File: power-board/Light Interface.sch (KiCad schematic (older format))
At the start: 20 parts, among them J3 CONN_01X04, J4 CONN_01X04, J5 CONN_01X04, J6 CONN_01X04, J7 CONN_01X04

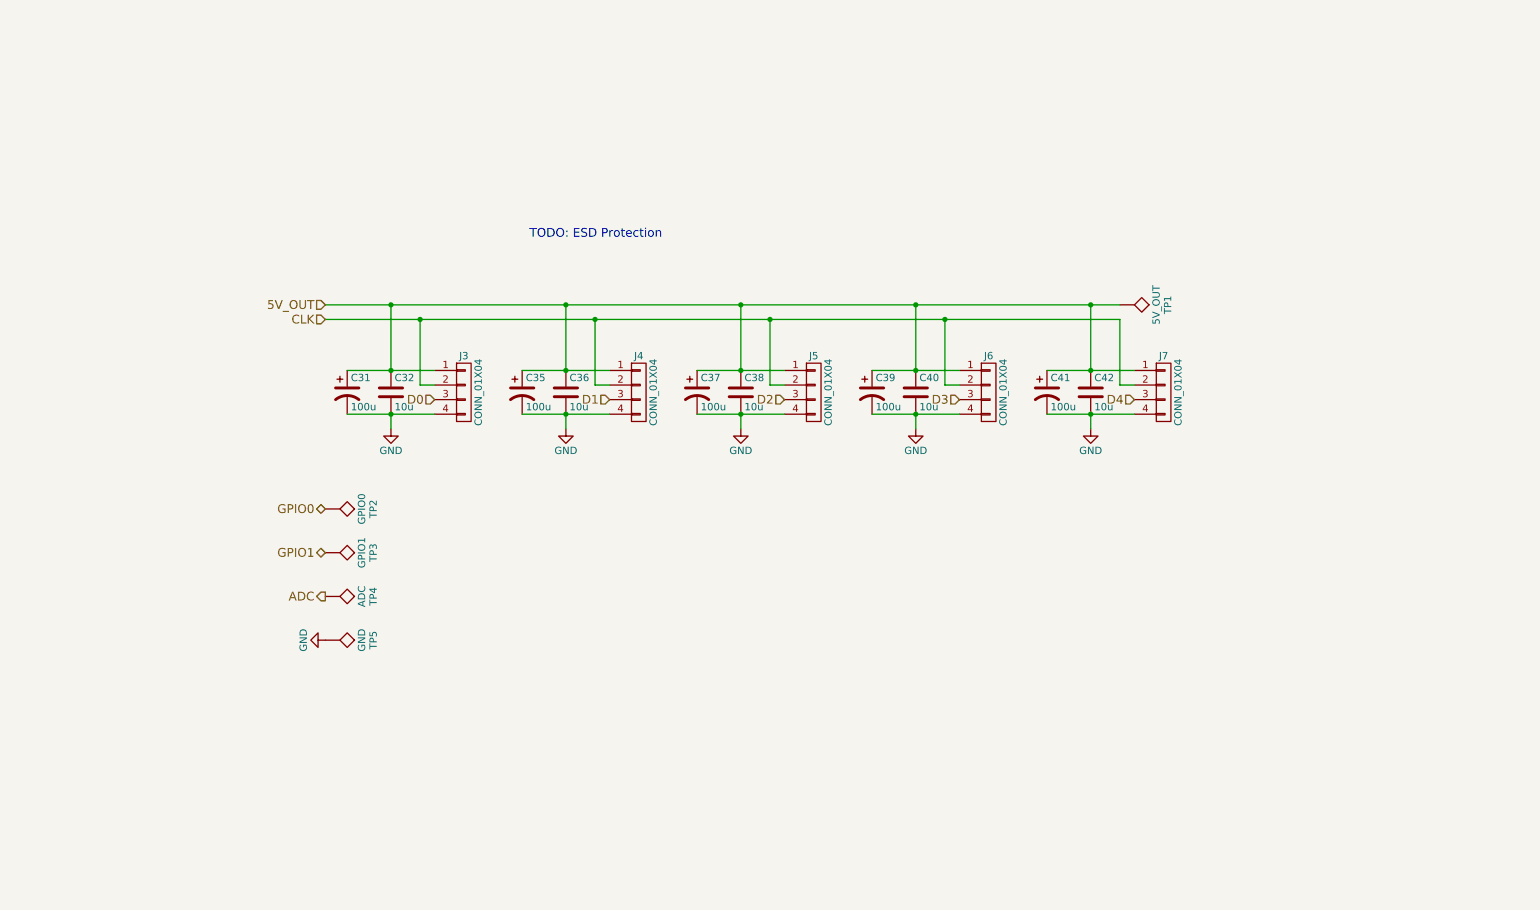
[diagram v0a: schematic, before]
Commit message: changed MCU to run at 3.3v
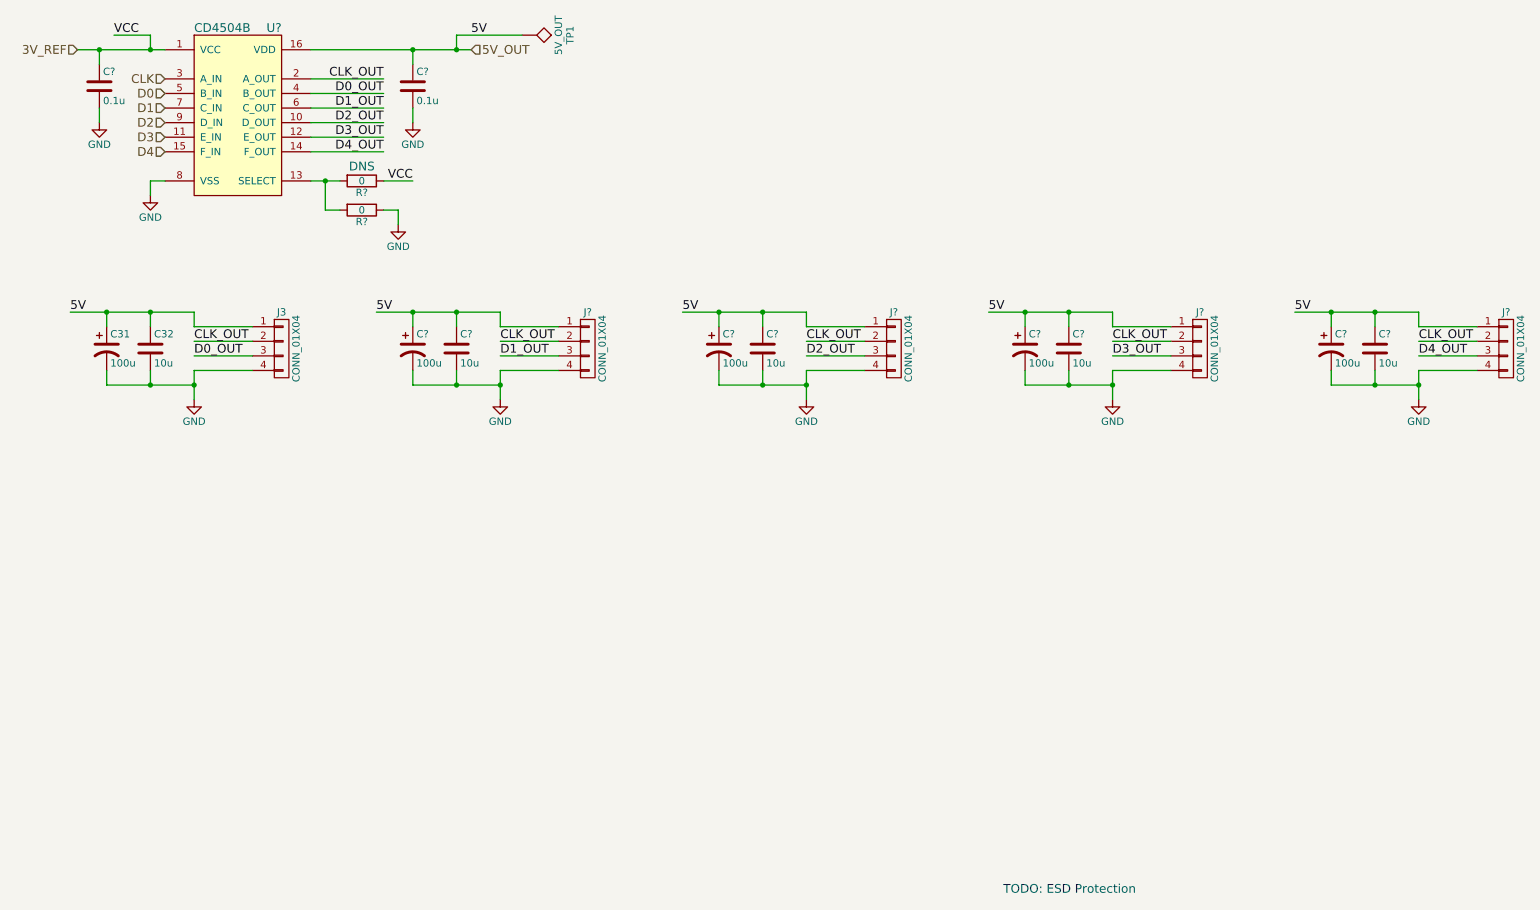
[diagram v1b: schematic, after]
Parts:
- removed C35, C37, C39, C41: 100u, symbol CP1
- removed C36, C38, C40, C42: 10u, symbol C
- removed J4, J5, J6, J7: CONN_01X04, symbol CONN_01X04
- removed TP2: GPIO0, symbol TEST
- removed TP3: GPIO1, symbol TEST
- removed TP4: ADC, symbol TEST
- removed TP5: GND, symbol TEST
- added C? (x2): 0.1u, symbol C
- added C? (x4): 10u, symbol C
- added C? (x4): 100u, symbol CP1
- added J? (x4): CONN_01X04, symbol CONN_01X04
- added R? (x2): 0, symbol R
- added U?: CD4504B, symbol CD4504B
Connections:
- net 5V_OUT: now also C?.1, C?.1, C?.1, C?.1, C?.1, C?.1, C?.1, C?.1, C?.1, J?.1 (P1), J?.1 (P1), J?.1 (P1), J?.1 (P1), U?.16 (VDD)
- net CLK: now also U?.3 (A_IN); no longer J3.2 (P2)
- net D0: now also U?.5 (B_IN); no longer J3.3 (P3)
- net D1: now also U?.7 (C_IN)
- net D2: now also U?.9 (D_IN)
- net D3: now also U?.11 (E_IN)
- net D4: now also U?.15 (F_IN)
- net GND: now also C?.2, C?.2, C?.2, C?.2, C?.2, C?.2, C?.2, C?.2, C?.2, C?.2, J?.4 (P4), J?.4 (P4), J?.4 (P4), J?.4 (P4), R?.1, U?.8 (VSS)
- new net: R?.2, R?.2, U?.13 (SELECT)
- new net 3V_REF: C?.1, R?.1, U?.1 (VCC)
- new net CLK_OUT: J3.2 (P2), J?.2 (P2), J?.2 (P2), J?.2 (P2), J?.2 (P2), U?.2 (A_OUT)
- new net D0_OUT: J3.3 (P3), U?.4 (B_OUT)
- new net D1_OUT: J?.3 (P3), U?.6 (C_OUT)
- new net D2_OUT: J?.3 (P3), U?.10 (D_OUT)
- new net D3_OUT: J?.3 (P3), U?.12 (E_OUT)
- new net D4_OUT: J?.3 (P3), U?.14 (F_OUT)
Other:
- moved on the sheet: C31, C32, J3, TP1

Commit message: switched to XMEGA A4U
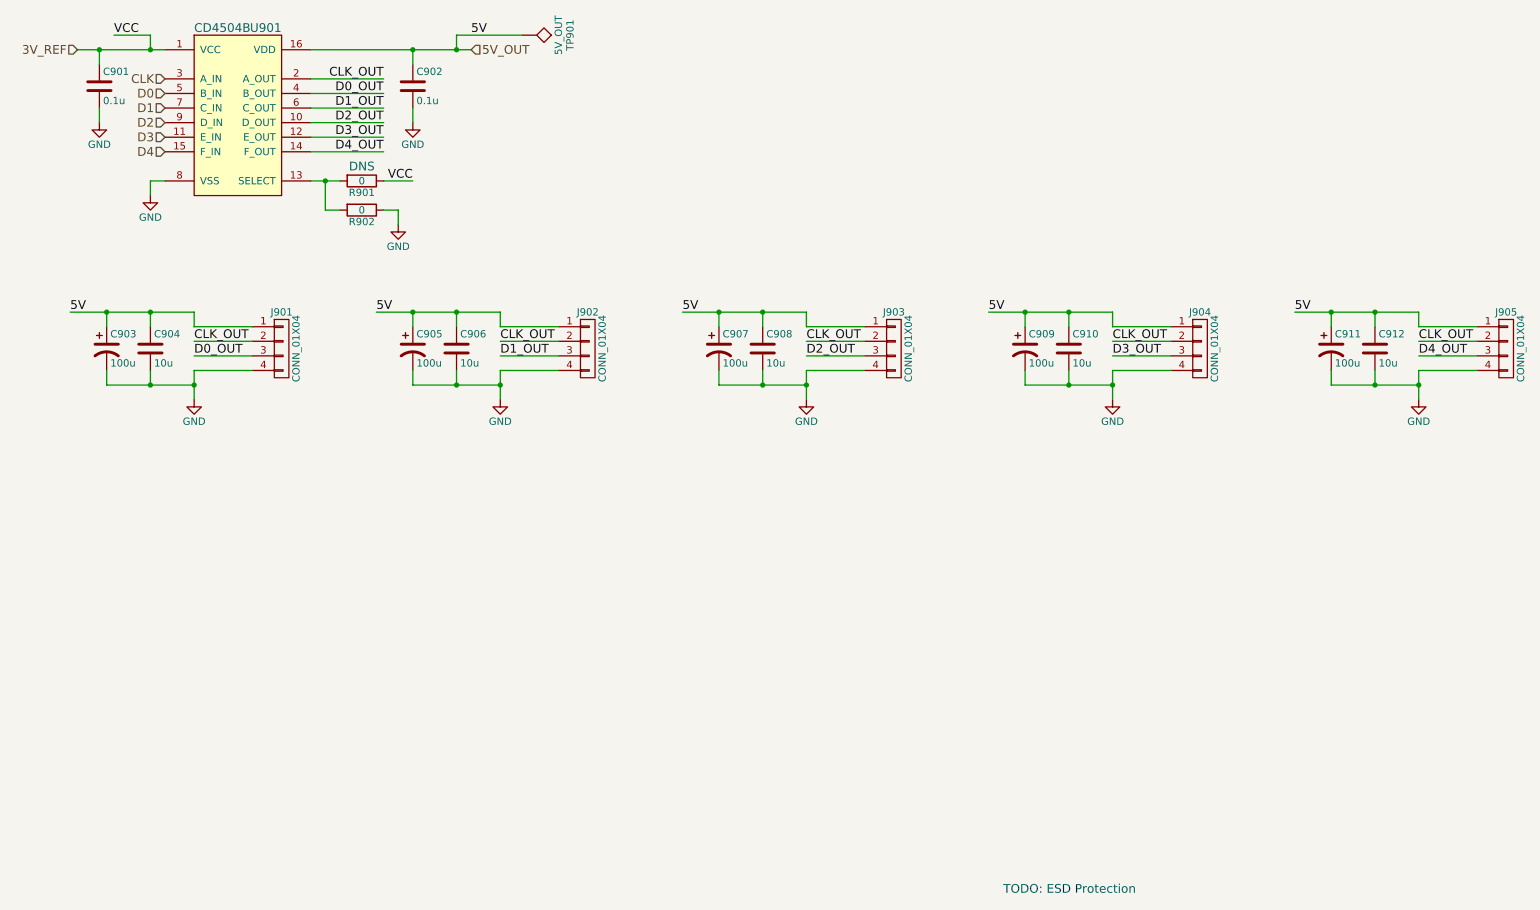
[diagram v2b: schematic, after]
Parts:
- gave numbers to parts that had none: 17
- renumbered C31 to C903, C32 to C904, J3 to J901, TP1 to TP901
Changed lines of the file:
@@
 $Descr A4 11693 8268
 encoding utf-8
-Sheet 9 10
+Sheet 9 11
 Title ""
 Date ""
@@
 CLK
 $Comp
-L CONN_01X04 J3
+L CONN_01X04 J901
 U 1 1 593A4988
 P 2300 2950
-F 0 "J3" H 2300 3200 50  0000 C CNN
+F 0 "J901" H 2300 3200 50  0000 C CNN
 F 1 "CONN_01X04" V 2400 2950 50  0000 C CNN
 F 2 "" H 2300 2950 50  0001 C CNN
@@
 $EndComp
 $Comp
-L C C32
+L C C904
 U 1 1 593A49E6
 P 1400 2950
-F 0 "C32" H 1425 3050 50  0000 L CNN
+F 0 "C904" H 1425 3050 50  0000 L CNN
 F 1 "10u" H 1425 2850 50  0000 L CNN
 F 2 "" H 1438 2800 50  0001 C CNN
@@
 $EndComp
 $Comp
-L CP1 C31
+L CP1 C903
 U 1 1 593A4A03
 P 1100 2950
-F 0 "C31" H 1125 3050 50  0000 L CNN
+F 0 "C903" H 1125 3050 50  0000 L CNN
 F 1 "100u" H 1125 2850 50  0000 L CNN
 F 2 "" H 1100 2950 50  0001 C CNN
@@
 $EndComp
 $Comp
-L GND #PWR37
+L GND #PWR045
 U 1 1 593A4A49
 P 1700 3300
-F 0 "#PWR37" H 1700 3050 50  0001 C CNN
+F 0 "#PWR045" H 1700 3050 50  0001 C CNN
 F 1 "GND" H 1700 3150 50  0000 C CNN
 F 2 "" H 1700 3300 50  0001 C CNN
@@
 	2100 2900 1700 2900
 $Comp
-L TEST TP1
+L TEST TP901
 U 1 1 593A5C05
 P 3950 800
-F 0 "TP1" H 3950 1100 50  0000 C BNN
+F 0 "TP901" H 3950 1100 50  0000 C BNN
 F 1 "5V_OUT" H 3950 1050 50  0000 C CNN
 F 2 "" H 3950 800 50  0001 C CNN
@@
 3V_REF
 $Comp
-L CD4504B U?
+L CD4504B U901
 U 1 1 593C5912
 P 1700 800
-F 0 "U?" H 2300 850 60  0000 R CNN
+F 0 "U901" H 2300 850 60  0000 R CNN
 F 1 "CD4504B" H 1700 850 60  0000 L CNN
 F 2 "" H 1750 950 60  0001 C CNN
@@
 	2100 2800 1700 2800
 Wire Wire Line
-	1700 2700 1700 2800
-Wire Wire Line
-	850  2700 1700 2700
+	1700 2800 1700 2700
+Wire Wire Line
+	1700 2700 850  2700
 Wire Wire Line
 	2100 3100 1700 3100
@@
 D4
 $Comp
-L GND #PWR?
+L GND #PWR046
 U 1 1 593C6AA7
 P 1400 1900
-F 0 "#PWR?" H 1400 1650 50  0001 C CNN
+F 0 "#PWR046" H 1400 1650 50  0001 C CNN
 F 1 "GND" H 1400 1750 50  0000 C CNN
 F 2 "" H 1400 1900 50  0001 C CNN
@@
 	1400 1800 1500 1800
 $Comp
-L C C?
+L C C901
 U 1 1 593C6AF5
 P 1050 1150
-F 0 "C?" H 1075 1250 50  0000 L CNN
+F 0 "C901" H 1075 1250 50  0000 L CNN
 F 1 "0.1u" H 1075 1050 50  0000 L CNN
 F 2 "" H 1088 1000 50  0001 C CNN
@@
 $EndComp
 $Comp
-L GND #PWR?
+L GND #PWR047
 U 1 1 593C6B4C
 P 1050 1400
-F 0 "#PWR?" H 1050 1150 50  0001 C CNN
+F 0 "#PWR047" H 1050 1150 50  0001 C CNN
 F 1 "GND" H 1050 1250 50  0000 C CNN
 F 2 "" H 1050 1400 50  0001 C CNN
@@
 Connection ~ 1050 900
 $Comp
-L C C?
+L C C902
 U 1 1 593C6C08
 P 3200 1150
-F 0 "C?" H 3225 1250 50  0000 L CNN
+F 0 "C902" H 3225 1250 50  0000 L CNN
 F 1 "0.1u" H 3225 1050 50  0000 L CNN
 F 2 "" H 3238 1000 50  0001 C CNN
@@
 $EndComp
 $Comp
-L GND #PWR?
+L GND #PWR048
 U 1 1 593C6C0E
 P 3200 1400
-F 0 "#PWR?" H 3200 1150 50  0001 C CNN
+F 0 "#PWR048" H 3200 1150 50  0001 C CNN
 F 1 "GND" H 3200 1250 50  0000 C CNN
 F 2 "" H 3200 1400 50  0001 C CNN
@@
 	3000 1600 2500 1600
 $Comp
-L CONN_01X04 J?
+L CONN_01X04 J902
 U 1 1 593C76E0
 P 4400 2950
-F 0 "J?" H 4400 3200 50  0000 C CNN
+F 0 "J902" H 4400 3200 50  0000 C CNN
 F 1 "CONN_01X04" V 4500 2950 50  0000 C CNN
 F 2 "" H 4400 2950 50  0001 C CNN
@@
 $EndComp
 $Comp
-L C C?
+L C C906
 U 1 1 593C76E8
 P 3500 2950
-F 0 "C?" H 3525 3050 50  0000 L CNN
+F 0 "C906" H 3525 3050 50  0000 L CNN
 F 1 "10u" H 3525 2850 50  0000 L CNN
 F 2 "" H 3538 2800 50  0001 C CNN
@@
 $EndComp
 $Comp
-L CP1 C?
+L CP1 C905
 U 1 1 593C76F0
 P 3200 2950
-F 0 "C?" H 3225 3050 50  0000 L CNN
+F 0 "C905" H 3225 3050 50  0000 L CNN
 F 1 "100u" H 3225 2850 50  0000 L CNN
 F 2 "" H 3200 2950 50  0001 C CNN
@@
 $EndComp
 $Comp
-L GND #PWR?
+L GND #PWR049
 U 1 1 593C76F6
 P 3800 3300
-F 0 "#PWR?" H 3800 3050 50  0001 C CNN
+F 0 "#PWR049" H 3800 3050 50  0001 C CNN
 F 1 "GND" H 3800 3150 50  0000 C CNN
 F 2 "" H 3800 3300 50  0001 C CNN
@@
 	4200 2800 3800 2800
 Wire Wire Line
-	3800 2700 3800 2800
-Wire Wire Line
-	2950 2700 3800 2700
+	3800 2800 3800 2700
+Wire Wire Line
+	3800 2700 2950 2700
 Wire Wire Line
 	4200 3100 3800 3100
@@
 D1_OUT
 $Comp
-L CONN_01X04 J?
+L CONN_01X04 J903
 U 1 1 593C797D
 P 6500 2950
-F 0 "J?" H 6500 3200 50  0000 C CNN
+F 0 "J903" H 6500 3200 50  0000 C CNN
 F 1 "CONN_01X04" V 6600 2950 50  0000 C CNN
 F 2 "" H 6500 2950 50  0001 C CNN
@@
 $EndComp
 $Comp
-L C C?
+L C C908
 U 1 1 593C7985
 P 5600 2950
-F 0 "C?" H 5625 3050 50  0000 L CNN
+F 0 "C908" H 5625 3050 50  0000 L CNN
 F 1 "10u" H 5625 2850 50  0000 L CNN
 F 2 "" H 5638 2800 50  0001 C CNN
@@
 $EndComp
 $Comp
-L CP1 C?
+L CP1 C907
 U 1 1 593C798D
 P 5300 2950
-F 0 "C?" H 5325 3050 50  0000 L CNN
+F 0 "C907" H 5325 3050 50  0000 L CNN
 F 1 "100u" H 5325 2850 50  0000 L CNN
 F 2 "" H 5300 2950 50  0001 C CNN
@@
 $EndComp
 $Comp
-L GND #PWR?
+L GND #PWR050
 U 1 1 593C7993
 P 5900 3300
-F 0 "#PWR?" H 5900 3050 50  0001 C CNN
+F 0 "#PWR050" H 5900 3050 50  0001 C CNN
 F 1 "GND" H 5900 3150 50  0000 C CNN
 F 2 "" H 5900 3300 50  0001 C CNN
@@
 	6300 2800 5900 2800
 Wire Wire Line
-	5900 2700 5900 2800
-Wire Wire Line
-	5050 2700 5900 2700
+	5900 2800 5900 2700
+Wire Wire Line
+	5900 2700 5050 2700
 Wire Wire Line
 	6300 3100 5900 3100
@@
 D2_OUT
 $Comp
-L CONN_01X04 J?
+L CONN_01X04 J904
 U 1 1 593C79B0
 P 8600 2950
-F 0 "J?" H 8600 3200 50  0000 C CNN
+F 0 "J904" H 8600 3200 50  0000 C CNN
 F 1 "CONN_01X04" V 8700 2950 50  0000 C CNN
 F 2 "" H 8600 2950 50  0001 C CNN
@@
 $EndComp
 $Comp
-L C C?
+L C C910
 U 1 1 593C79B8
 P 7700 2950
-F 0 "C?" H 7725 3050 50  0000 L CNN
+F 0 "C910" H 7725 3050 50  0000 L CNN
 F 1 "10u" H 7725 2850 50  0000 L CNN
 F 2 "" H 7738 2800 50  0001 C CNN
@@
 $EndComp
 $Comp
-L CP1 C?
+L CP1 C909
 U 1 1 593C79C0
 P 7400 2950
-F 0 "C?" H 7425 3050 50  0000 L CNN
+F 0 "C909" H 7425 3050 50  0000 L CNN
 F 1 "100u" H 7425 2850 50  0000 L CNN
 F 2 "" H 7400 2950 50  0001 C CNN
@@
 $EndComp
 $Comp
-L GND #PWR?
+L GND #PWR051
 U 1 1 593C79C6
 P 8000 3300
-F 0 "#PWR?" H 8000 3050 50  0001 C CNN
+F 0 "#PWR051" H 8000 3050 50  0001 C CNN
 F 1 "GND" H 8000 3150 50  0000 C CNN
 F 2 "" H 8000 3300 50  0001 C CNN
@@
 	8400 2800 8000 2800
 Wire Wire Line
-	8000 2700 8000 2800
-Wire Wire Line
-	7150 2700 8000 2700
+	8000 2800 8000 2700
+Wire Wire Line
+	8000 2700 7150 2700
 Wire Wire Line
 	8400 3100 8000 3100
@@
 D3_OUT
 $Comp
-L CONN_01X04 J?
+L CONN_01X04 J905
 U 1 1 593C7ADB
 P 10700 2950
-F 0 "J?" H 10700 3200 50  0000 C CNN
+F 0 "J905" H 10700 3200 50  0000 C CNN
 F 1 "CONN_01X04" V 10800 2950 50  0000 C CNN
 F 2 "" H 10700 2950 50  0001 C CNN
@@
 $EndComp
 $Comp
-L C C?
+L C C912
 U 1 1 593C7AE3
 P 9800 2950
-F 0 "C?" H 9825 3050 50  0000 L CNN
+F 0 "C912" H 9825 3050 50  0000 L CNN
 F 1 "10u" H 9825 2850 50  0000 L CNN
 F 2 "" H 9838 2800 50  0001 C CNN
@@
 $EndComp
 $Comp
-L CP1 C?
+L CP1 C911
 U 1 1 593C7AEB
 P 9500 2950
-F 0 "C?" H 9525 3050 50  0000 L CNN
+F 0 "C911" H 9525 3050 50  0000 L CNN
 F 1 "100u" H 9525 2850 50  0000 L CNN
 F 2 "" H 9500 2950 50  0001 C CNN
@@
 $EndComp
 $Comp
-L GND #PWR?
+L GND #PWR052
 U 1 1 593C7AF1
 P 10100 3300
-F 0 "#PWR?" H 10100 3050 50  0001 C CNN
+F 0 "#PWR052" H 10100 3050 50  0001 C CNN
 F 1 "GND" H 10100 3150 50  0000 C CNN
 F 2 "" H 10100 3300 50  0001 C CNN
@@
 	10500 2800 10100 2800
 Wire Wire Line
-	10100 2700 10100 2800
-Wire Wire Line
-	9250 2700 10100 2700
+	10100 2800 10100 2700
+Wire Wire Line
+	10100 2700 9250 2700
 Wire Wire Line
 	10500 3100 10100 3100
@@
 D4_OUT
 $Comp
-L R R?
+L R R901
 U 1 1 593B6E24
 P 2850 1800
-F 0 "R?" V 2930 1800 50  0000 C CNN
+F 0 "R901" V 2930 1800 50  0000 C CNN
 F 1 "0" V 2850 1800 50  0000 C CNN
 F 2 "" V 2780 1800 50  0001 C CNN
@@
 $EndComp
 $Comp
-L R R?
+L R R902
 U 1 1 593B6EB2
 P 2850 2000
-F 0 "R?" V 2930 2000 50  0000 C CNN
+F 0 "R902" V 2930 2000 50  0000 C CNN
 F 1 "0" V 2850 2000 50  0000 C CNN
 F 2 "" V 2780 2000 50  0001 C CNN
@@
 Connection ~ 2600 1800
 $Comp
-L GND #PWR?
+L GND #PWR053
 U 1 1 593B71E9
 P 3100 2100
-F 0 "#PWR?" H 3100 1850 50  0001 C CNN
+F 0 "#PWR053" H 3100 1850 50  0001 C CNN
 F 1 "GND" H 3100 1950 50  0000 C CNN
 F 2 "" H 3100 2100 50  0001 C CNN

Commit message: routed board
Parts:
- removed C903, C905, C907, C909, C911: 100u, symbol CP1
- removed TP901: 5V_OUT, symbol TEST
- C901, C902: footprint (none) -> Capacitors_SMD:C_0603; MFG (none) -> Murata Electronics; MPN (none) -> GRM188R71H104KA93D
- C904, C906, C908, C910, C912: footprint (none) -> Capacitors_SMD:C_0805
- J901, J902, J903, J904, J905: footprint (none) -> Connectors_Terminal_Blocks:TerminalBlock_Pheonix_PT-3.5mm_4pol
- R901, R902: footprint (none) -> Resistors_SMD:R_0603
- U901: footprint (none) -> Housings_SOIC:SOIC-16_3.9x9.9mm_Pitch1.27mm; MFG (none) -> Texas Instruments; MPN (none) -> CD4504BM96
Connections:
- wire segments 84 -> 82

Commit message: adding more part numbers
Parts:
- R901, R902: MFG (none) -> Yageo; MPN (none) -> RC0603JR-070RL
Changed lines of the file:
@@
 F 3 "" H 2850 1800 50  0001 C CNN
 F 4 "DNS" V 2750 1800 60  0000 C CNN "Note"
+F 5 "Yageo" V 2850 1800 60  0001 C CNN "MFG"
+F 6 "RC0603JR-070RL" V 2850 1800 60  0001 C CNN "MPN"
 	1    2850 1800
 	0    1    1    0
@@
 F 2 "Resistors_SMD:R_0603" V 2780 2000 50  0001 C CNN
 F 3 "" H 2850 2000 50  0001 C CNN
+F 4 "Yageo" V 2850 2000 60  0001 C CNN "MFG"
+F 5 "RC0603JR-070RL" V 2850 2000 60  0001 C CNN "MPN"
 	1    2850 2000
 	0    1    1    0
